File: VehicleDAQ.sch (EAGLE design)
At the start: 15 parts, among them IC1 786TV, IC3 78L05Z, X1 RASPI_BOARD_B+_FP

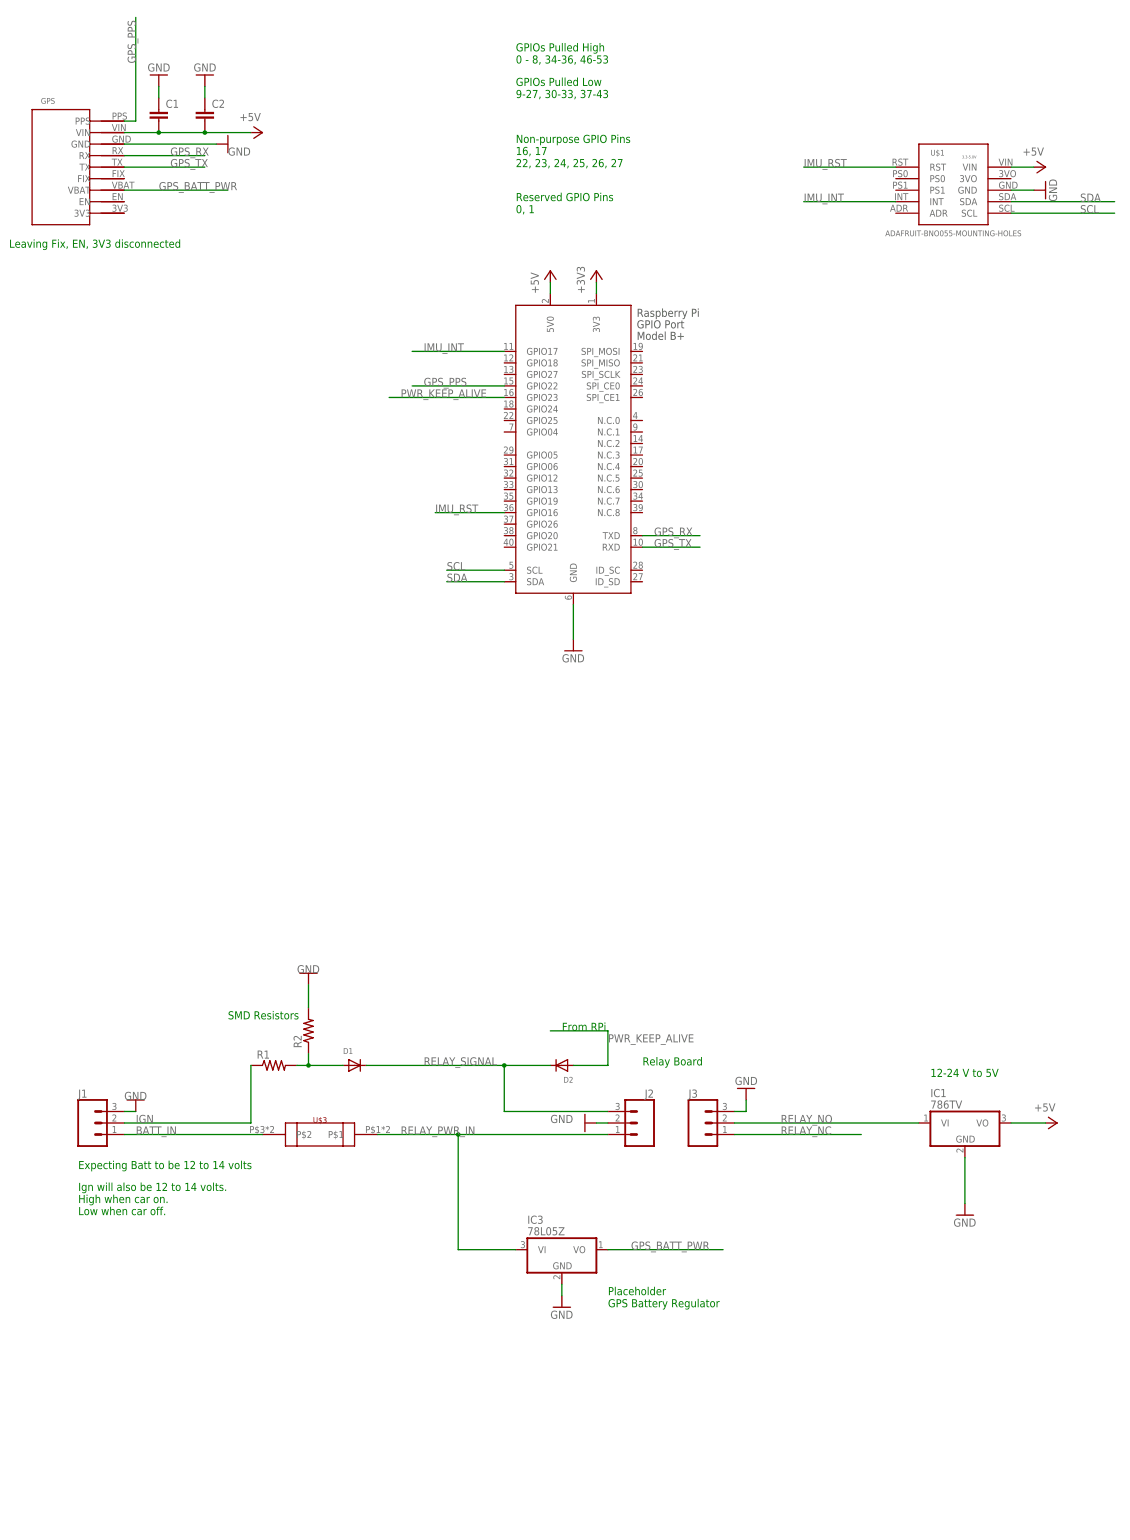
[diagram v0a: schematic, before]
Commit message: Added actual regulators and capacitors.  All surface mount caps and regulators.
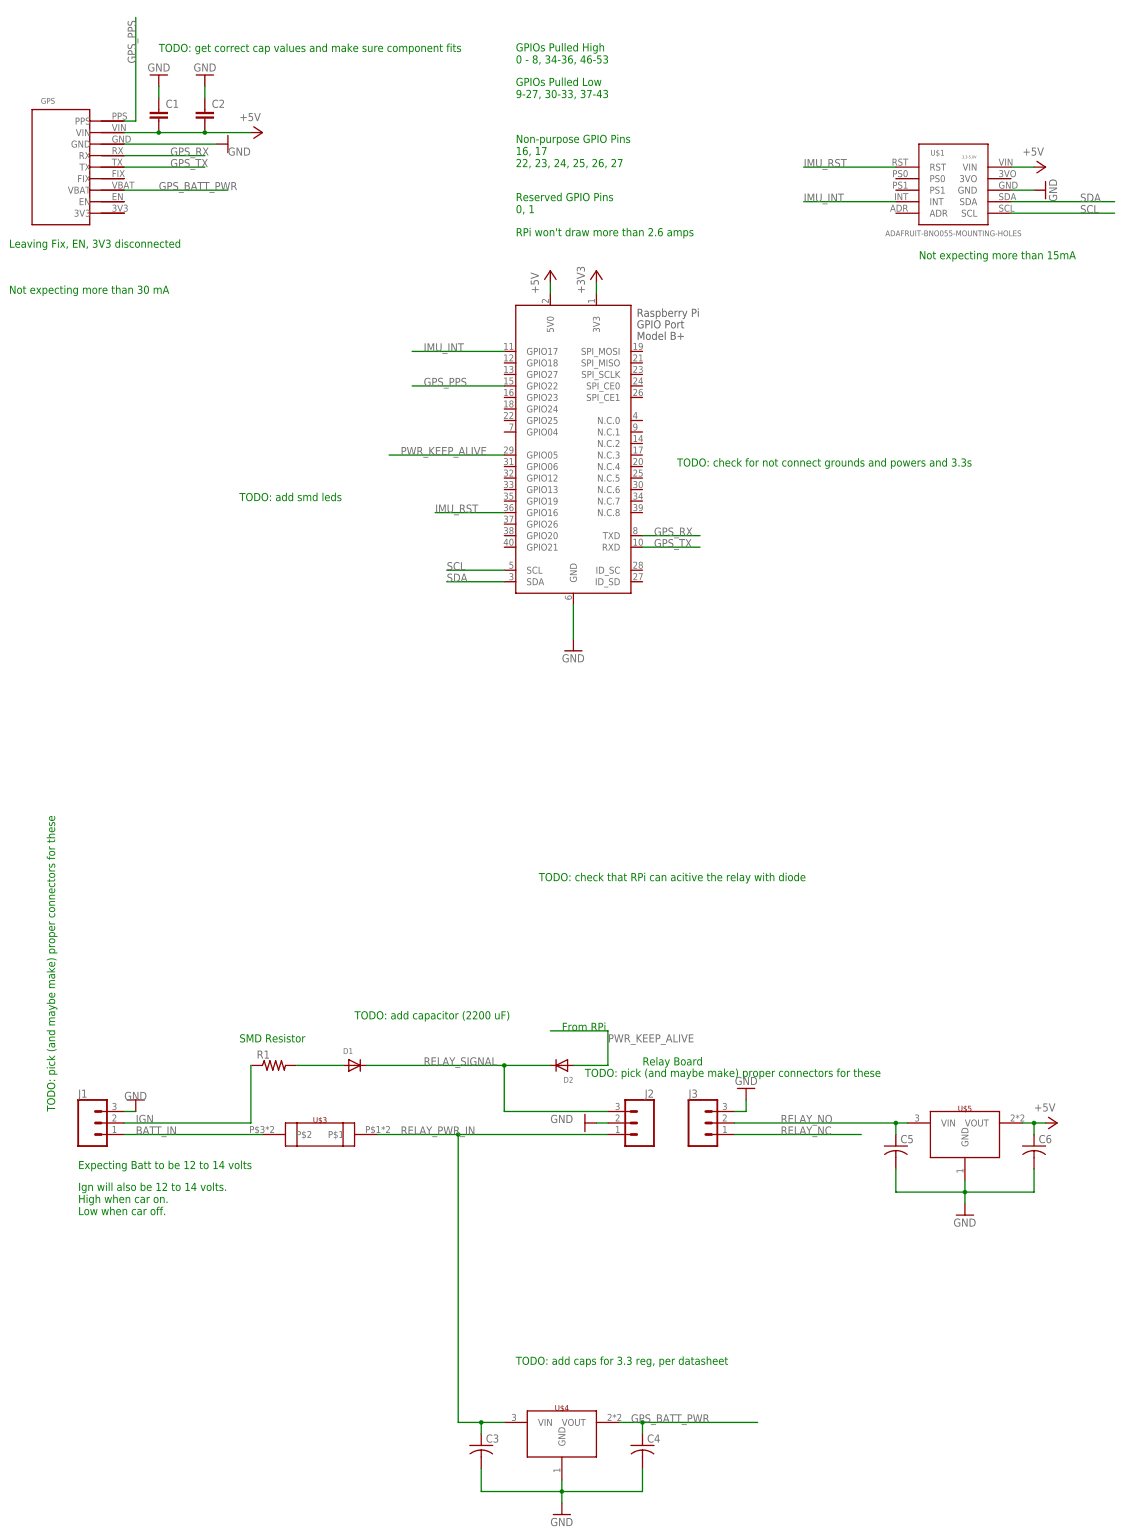
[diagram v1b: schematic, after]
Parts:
- removed IC1: 786TV, linear:786TV
- removed IC3: 78L05Z, adafruit:78L05Z
- removed R2: (no value), rcl:R-US_R1206W
- added C3, C4, C5, C6: (no value), adafruit:C-USC1206K
- added U$4, U$5: LD1085D2M33R_REGULATOR, keverly:LD1085D2M33R_REGULATOR
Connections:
- net +5V: now also C6.1, U$5.VOUT; no longer IC1.VO
- net GND: now also C3.2, C4.2, C5.2, C6.2, U$4.GND, U$5.GND; no longer IC1.GND, IC3.GND, R2.2
- net GPS_BATT_PWR: now also C4.1, U$4.VOUT; no longer IC3.VO
- net N$1: no longer R2.1
- net PWR_KEEP_ALIVE: now also X1.GPIO05; no longer X1.GPIO23
- net RELAY_NO: now also C5.1, U$5.VIN; no longer IC1.VI
- net RELAY_PWR_IN: now also C3.1, U$4.VIN; no longer IC3.VI
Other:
- note added: "Not expecting more than 15mA"
- note added: "Not expecting more than 30 mA"
- note added: "RPi won't draw more than 2.6 amps"
- note added: "SMD Resistor"
- note added: "TODO: add capacitor (2200 uF)"
- note added: "TODO: add caps for 3.3 reg, per datasheet"
- note added: "TODO: add smd leds"
- note added: "TODO: check for not connect grounds and powers and 3.3s"
- note added: "TODO: check that RPi can acitive the relay with diode"
- note added: "TODO: get correct cap values and make sure component fits"
- note added: "TODO: pick (and maybe make) proper connectors for these"
- note removed: "12-24 V to 5V"
- note removed: "Placeholder GPS Battery Regulator"
- note removed: "SMD Resistors"
